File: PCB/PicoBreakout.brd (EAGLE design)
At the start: 88.9 x 57.1 mm, 43 parts

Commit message: updated run trace
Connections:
- new net N$64: JP1.20, X1.RUN
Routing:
- net N$64: track 0.00 -> 54.4 mm
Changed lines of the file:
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@@
 </layers>
 <board>
-<fusionsync huburn="a.cGVyc29uYWw6dWUyY2VjZDkz" projecturn="a.cGVyc29uYWw6dWUyY2VjZDkzIzIwMTkwMTAzMTY4MjEzNTA2" f3durn="urn:adsk.wipprod:dm.lineage:g2FzlmCfS4iXO2IOv7ZSYg" pcbguid="89c8c0a1-dd69-4ef4-b93a-1f64f55537e1" lastpulledtime="" lastsyncedchangeguid="" latestrevisionid="3ed4198d-4a7d-471d-a0de-3c94c9aa8158" lastsyncedrevisionid="3ed4198d-4a7d-471d-a0de-3c94c9aa8158" lastboardhashguid="849b84f2-fd19-473c-12fe-b8a419a203dc" lastpushedtime="2023-01-17T13:23:22Z" linktopcb3d="true"/>
+<fusionsync huburn="a.cGVyc29uYWw6dWUyY2VjZDkz" projecturn="a.cGVyc29uYWw6dWUyY2VjZDkzIzIwMTkwMTAzMTY4MjEzNTA2" f3durn="urn:adsk.wipprod:dm.lineage:g2FzlmCfS4iXO2IOv7ZSYg" pcbguid="" lastpulledtime="" lastsyncedchangeguid="" latestrevisionid="3ed4198d-4a7d-471d-a0de-3c94c9aa8158" lastsyncedrevisionid="3ed4198d-4a7d-471d-a0de-3c94c9aa8158" lastboardhashguid="849b84f2-fd19-473c-12fe-b8a419a203dc" lastpushedtime="2023-01-17T13:23:22Z" linktopcb3d="false"/>
 <plain>
 <text x="37.587415625" y="7.9738875" size="1.016" layer="27" rot="R90">100k</text>
@@
 <contactref element="JP1" pad="7"/>
 <wire x1="58.495415625" y1="25.6468875" x2="62.7181625" y2="25.6468875" width="0.4572" layer="1"/>
-<wire x1="66.454171875" y1="29.382896875" x2="66.454171875" y2="41.8084375" width="0.4572" layer="1"/>
+<wire x1="67.066525" y1="29.99525" x2="67.066525" y2="42.420790625" width="0.4572" layer="1"/>
 <wire x1="77.485671875" y1="45.69934375" x2="70.345078125" y2="45.69934375" width="0.4572" layer="1"/>
-<wire x1="70.345078125" y1="45.69934375" x2="66.454171875" y2="41.8084375" width="0.4572" layer="1"/>
-<wire x1="62.7181625" y1="25.6468875" x2="66.454171875" y2="29.382896875" width="0.4572" layer="1"/>
+<wire x1="70.345078125" y1="45.69934375" x2="67.066525" y2="42.420790625" width="0.4572" layer="1"/>
+<wire x1="62.7181625" y1="25.6468875" x2="67.066525" y2="29.99525" width="0.4572" layer="1"/>
 </signal>
 <signal name="N$28">
@@
 <wire x1="75.59078125" y1="8.902146875" x2="78.912853125" y2="8.902146875" width="0.4572" layer="16"/>
 </signal>
+<signal name="N$64">
+<contactref element="X1" pad="RUN"/>
+<contactref element="JP1" pad="20"/>
+<wire x1="58.495415625" y1="28.1868875" x2="62.302409375" y2="28.1868875" width="0.4572" layer="1"/>
+<wire x1="62.302409375" y1="28.1868875" x2="65.9900875" y2="31.874565625" width="0.4572" layer="1"/>
+<wire x1="65.9900875" y1="31.874565625" x2="65.9900875" y2="43.0162375" width="0.4572" layer="1"/>
+<wire x1="65.9900875" y1="43.0162375" x2="69.924359375" y2="46.950509375" width="0.4572" layer="1"/>
+<wire x1="81.041940625" y1="46.950509375" x2="81.839234375" y2="46.153215625" width="0.4572" layer="1"/>
+<wire x1="81.839234375" y1="46.153215625" x2="81.839234375" y2="32.27290625" width="0.4572" layer="1"/>
+<wire x1="81.839234375" y1="32.27290625" x2="80.025671875" y2="30.45934375" width="0.4572" layer="1"/>
+<wire x1="69.924359375" y1="46.950509375" x2="81.041940625" y2="46.950509375" width="0.4572" layer="1"/>
+</signal>
 </signals>

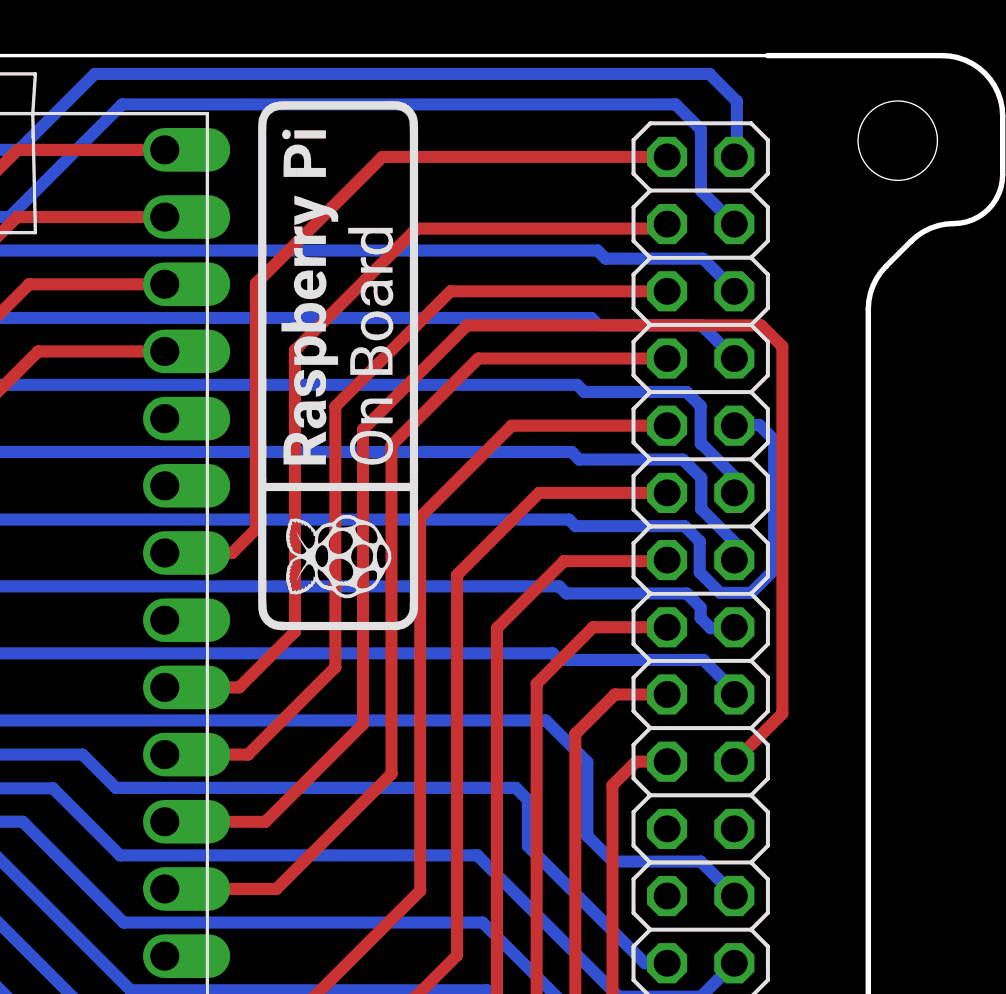
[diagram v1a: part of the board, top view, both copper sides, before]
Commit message: updated pico board
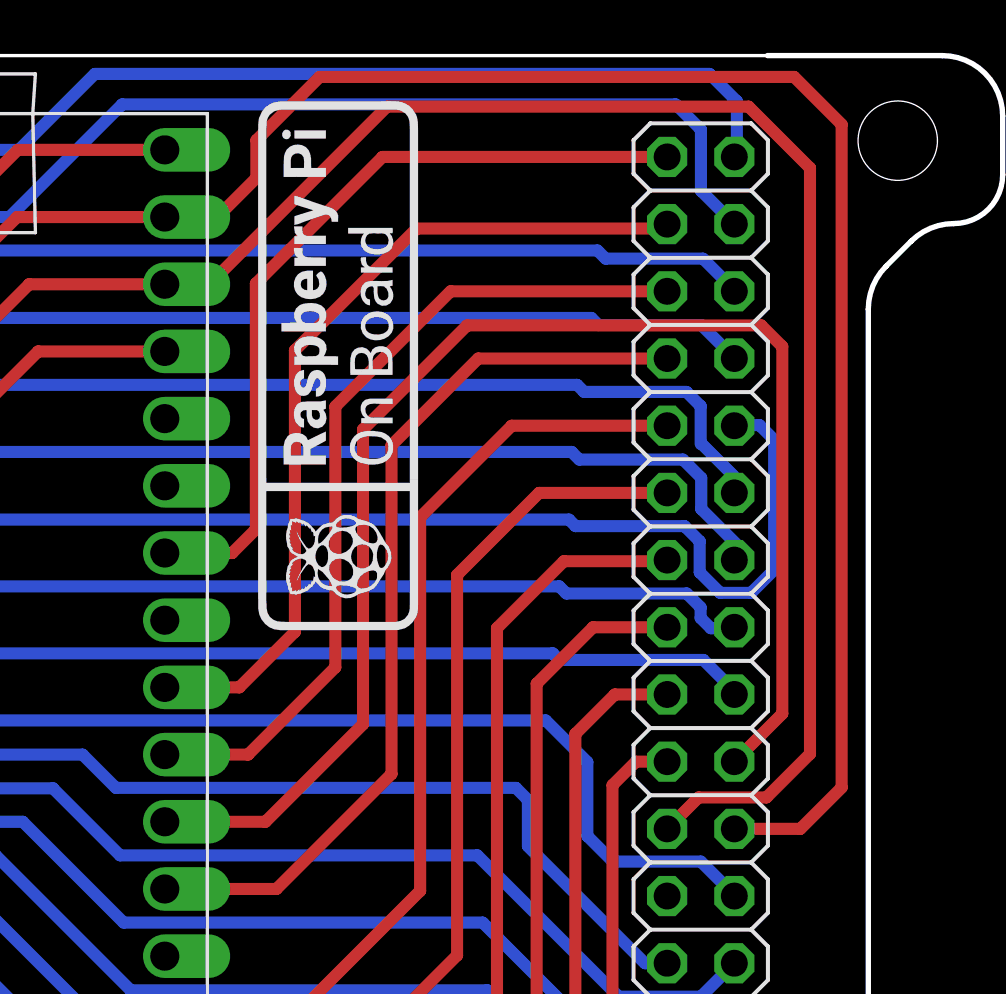
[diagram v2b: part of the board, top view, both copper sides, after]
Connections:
- net N$19: now also JP1.21
- net N$20: now also JP1.22
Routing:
- net N$20: track 74.0 -> 133.1 mm
- net N$19: track 62.1 -> 118.9 mm
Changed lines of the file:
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@@
 <wire x1="47.848415625" y1="25.0738875" x2="47.848415625" y2="42.9858875" width="0.4572" layer="1"/>
 <wire x1="47.848415625" y1="42.9858875" x2="53.369415625" y2="48.5068875" width="0.4572" layer="1"/>
+<contactref element="JP1" pad="21"/>
+<wire x1="77.485671875" y1="27.91934375" x2="78.673434375" y2="29.10710625" width="0.4572" layer="1"/>
+<wire x1="82.88615" y1="30.752925" x2="82.88615" y2="52.901603125" width="0.4572" layer="1"/>
+<wire x1="82.88615" y1="52.901603125" x2="80.566559375" y2="55.22119375" width="0.4572" layer="1"/>
+<wire x1="60.183940625" y1="48.5068875" x2="58.495415625" y2="48.5068875" width="0.4572" layer="1"/>
+<wire x1="78.673434375" y1="29.10710625" x2="81.24033125" y2="29.10710625" width="0.4572" layer="1"/>
+<wire x1="81.24033125" y1="29.10710625" x2="82.88615" y2="30.752925" width="0.4572" layer="1"/>
+<wire x1="80.566559375" y1="55.22119375" x2="66.898246875" y2="55.22119375" width="0.4572" layer="1"/>
+<wire x1="66.898246875" y1="55.22119375" x2="60.183940625" y2="48.5068875" width="0.4572" layer="1"/>
 <wire x1="31.982415625" y1="9.7078875" x2="31.700415625" y2="9.9118875" width="0" layer="19" extent="1-1"/>
 </signal>
@@
 <wire x1="26.662415625" y1="9.0318875" x2="26.662415625" y2="10.9708875" width="0.4572" layer="1"/>
 <wire x1="26.662415625" y1="10.9708875" x2="28.319415625" y2="12.6278875" width="0.4572" layer="1"/>
+<contactref element="JP1" pad="22"/>
+<wire x1="80.025671875" y1="27.91934375" x2="82.52129375" y2="27.91934375" width="0.4572" layer="1"/>
+<wire x1="84.08198125" y1="29.48003125" x2="84.08198125" y2="54.547765625" width="0.4572" layer="1"/>
+<wire x1="84.08198125" y1="54.547765625" x2="82.286171875" y2="56.343575" width="0.4572" layer="1"/>
+<wire x1="82.286171875" y1="56.343575" x2="64.35074375" y2="56.343575" width="0.4572" layer="1"/>
+<wire x1="64.35074375" y1="56.343575" x2="61.959078125" y2="53.951909375" width="0.4572" layer="1"/>
+<wire x1="61.959078125" y1="53.951909375" x2="61.959078125" y2="52.527478125" width="0.4572" layer="1"/>
+<wire x1="61.959078125" y1="52.527478125" x2="60.4784875" y2="51.0468875" width="0.4572" layer="1"/>
+<wire x1="60.4784875" y1="51.0468875" x2="58.495415625" y2="51.0468875" width="0.4572" layer="1"/>
+<wire x1="82.52129375" y1="27.91934375" x2="84.08198125" y2="29.48003125" width="0.4572" layer="1"/>
 <wire x1="28.319415625" y1="12.6278875" x2="31.926415625" y2="20.0728875" width="0" layer="19" extent="1-1"/>
 </signal>
